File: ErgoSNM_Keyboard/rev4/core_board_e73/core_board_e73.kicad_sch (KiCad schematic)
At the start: 55 parts, among them J1 USB_C_Receptacle_USB2.0, J2 USB_C_Receptacle_USB2.0, J3 Conn_01x30, J4 Conn_Batt, J5 Debug, SW1 SW_DPDT_x2, U1 E73-2G4M08S1C, U2 SRV05-4, U3 TPS63020, U4 BQ24075RGT, U5 SRV05-4, Y1 32.768kHz

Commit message: feat: update USB ESD
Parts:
- removed R1, R2: 27R, Resistor_SMD:R_0402_1005Metric, symbol Device:R
- removed U2, U5: SRV05-4, Package_TO_SOT_SMD:SOT-23-6, symbol Power_Protection:SRV05-4
- added C1: 4.7nF, Capacitor_SMD:C_0805_2012Metric, symbol Device:C_Small
- added C4: 100nF, Capacitor_SMD:C_0402_1005Metric, symbol Device:C_Small
- added R1: 1M, Resistor_SMD:R_0603_1608Metric, symbol Device:R_Small
- added U2, U5: USBLC6-2SC6, Package_TO_SOT_SMD:SOT-23-6, symbol Power_Protection:USBLC6-2SC6
- R3, R4: value 5.1k -> 5.1k 1%
- renumbered C8 to C10, C9 to C11, C10 to C12, C11 to C13, C12 to C14, C13 to C15, C14 to C16, C15 to C17, C16 to C18, C17 to C19, C1 to C2, C2 to C3, C3 to C5, C4 to C6, C5 to C7, C6 to C8, C7 to C9, R14 to R2
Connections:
- net D+ is gone; now on net USB_D+: U1.31 (D+)
- net D- is gone; now on net USB_D-: U1.29 (D-)
- net GND: now also C1.2, C4.1, R1.2, U2.2 (GND), U5.2 (GND); no longer J1.S1 (SHIELD)
- net RX: now also U5.6 (I/O1); no longer J2.A7 (D-), J2.B7 (D-)
- net TX: now also U5.4 (I/O2); no longer J2.A6 (D+), J2.B6 (D+)
- net USB_D+: now also U2.4 (I/O2); no longer J1.A6 (D+), J1.B6 (D+)
- net USB_D-: now also U2.6 (I/O1); no longer J1.A7 (D-), J1.B7 (D-)
- net VBUS: now also C4.2, U2.5 (VBUS), U5.5 (VBUS)
- new net: J2.A6 (D+), J2.B6 (D+), U5.3 (I/O2)
- new net: J2.A7 (D-), J2.B7 (D-), U5.1 (I/O1)
- new net CONN_D+: J1.A6 (D+), J1.B6 (D+), U2.3 (I/O2)
- new net CONN_D-: J1.A7 (D-), J1.B7 (D-), U2.1 (I/O1)
- new net USB_SH: C1.1, J1.S1 (SHIELD), R1.1
- no-connect marks 28 -> 24
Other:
- note added: "Refer to Nordic nRF52833-DK 4.7nF 10V"

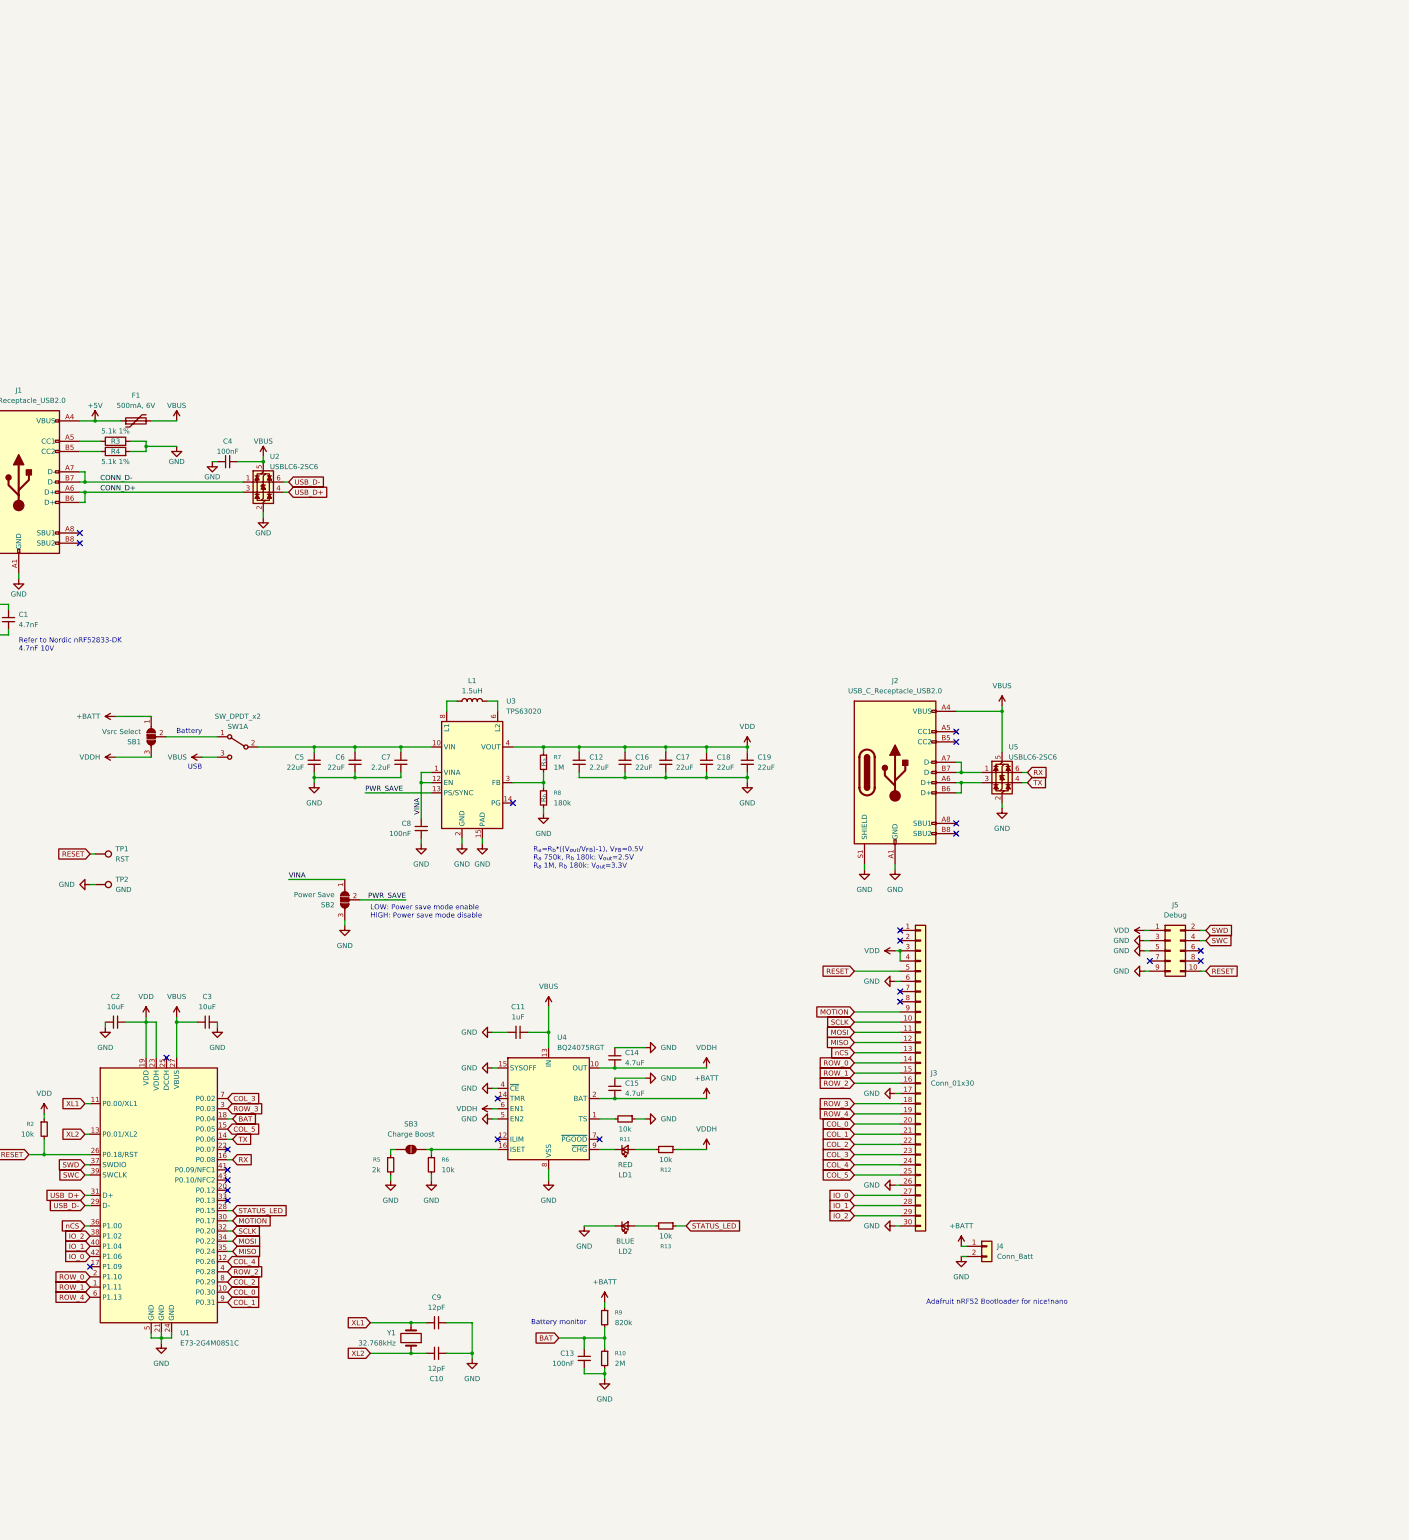
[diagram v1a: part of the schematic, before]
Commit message: feat: change Buck-Boost DC/DC IC from TPS63020 to TPS63900
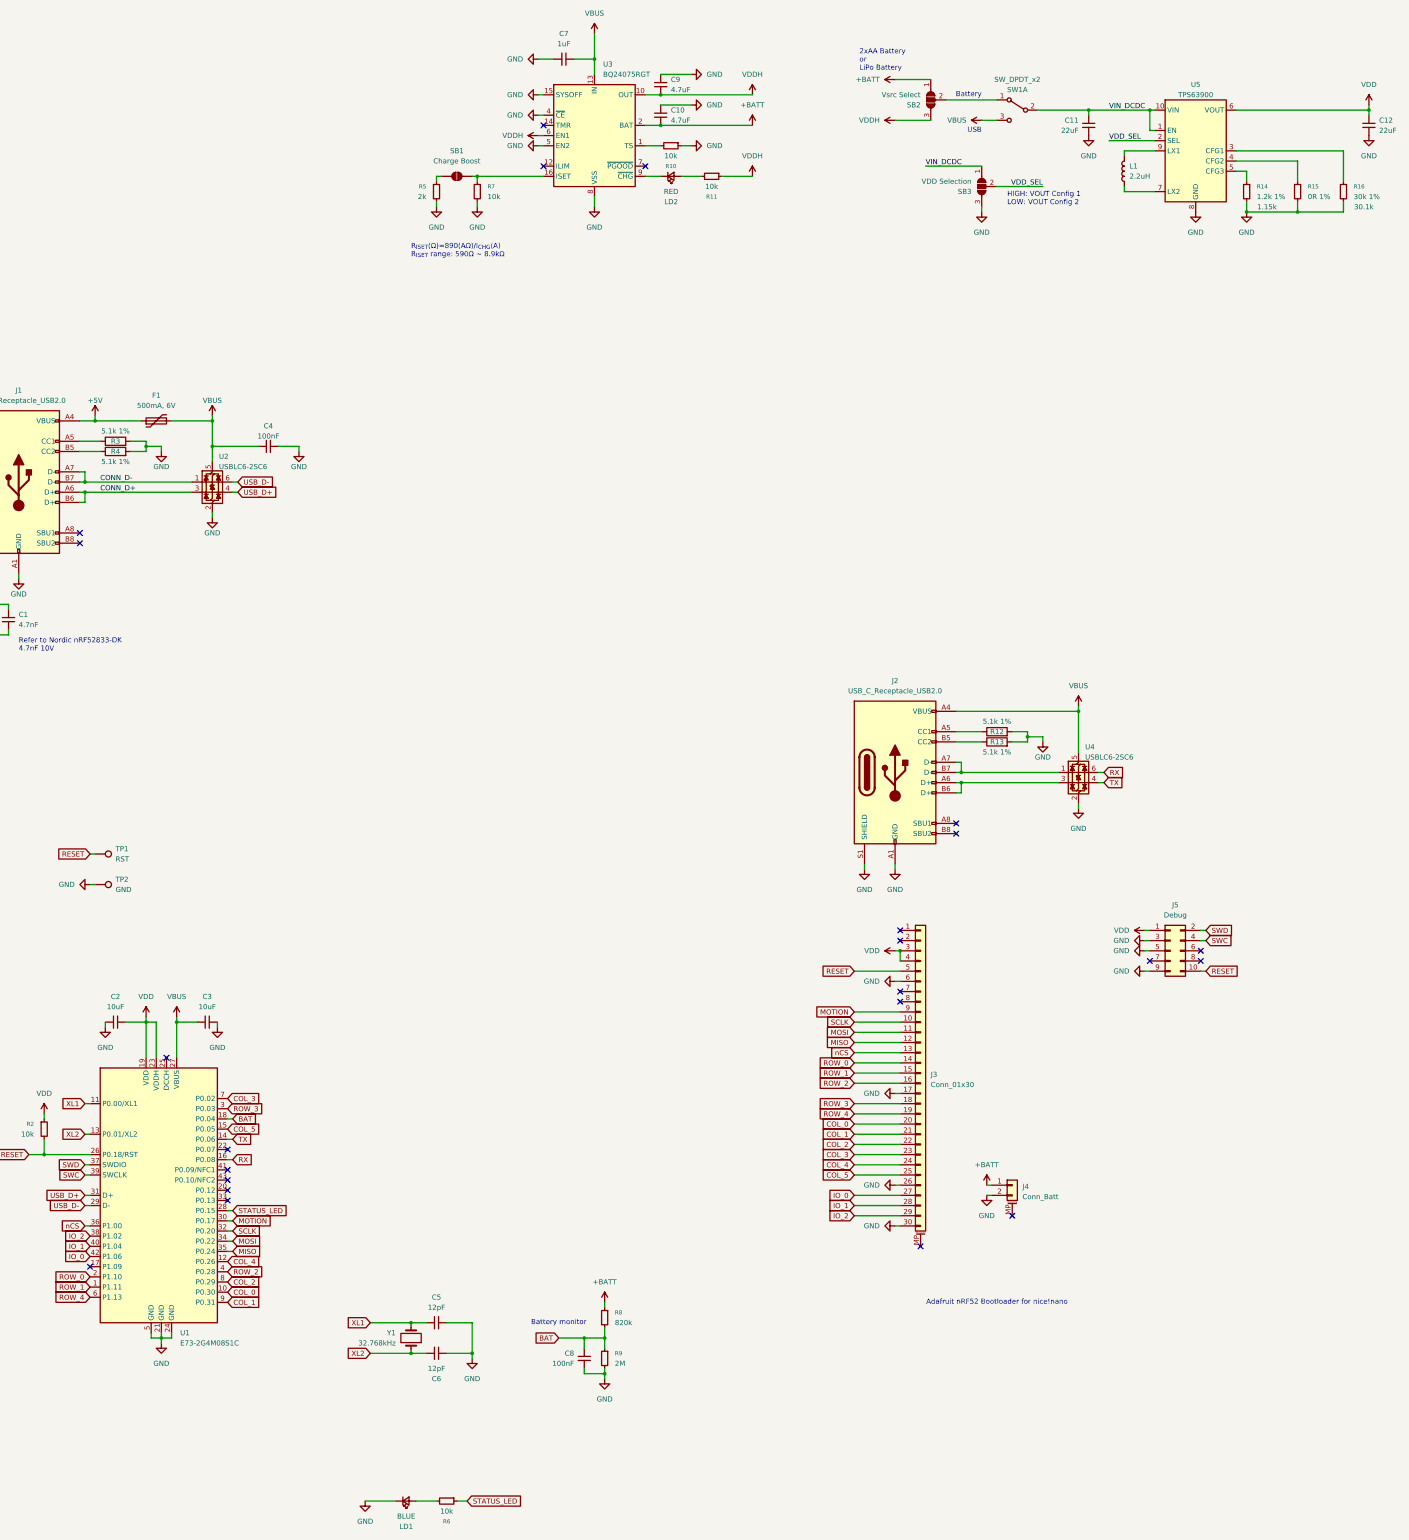
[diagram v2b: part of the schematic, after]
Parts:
- removed C16, C17, C18, C19, C5, C6: 22uF, Capacitor_SMD:C_0805_2012Metric, symbol Device:C_Small
- removed C7: 2.2uF, Capacitor_SMD:C_0603_1608Metric, symbol Device:C_Small
- removed C8: 100nF, Capacitor_SMD:C_0402_1005Metric, symbol Device:C_Small
- removed J4: Conn_Batt, Connector_JST:JST_PH_S2B-PH-SM4-TB_1x02-1MP_P2.00mm_Horizontal, symbol Connector_Generic:Conn_01x02
- removed R7: 1M, Resistor_SMD:R_0402_1005Metric, symbol Device:R_Small
- removed R8: 180k, Resistor_SMD:R_0402_1005Metric, symbol Device:R_Small
- removed U3: TPS63020, Package_SON:VSON-14-1EP_3x4.45mm_P0.65mm_EP1.6x4.2mm_ThermalVias, symbol ErgoSNM_Keyboard_Library:TPS63020
- added C11: 22uF, Capacitor_SMD:C_0805_2012Metric, symbol Device:C_Small
- added J4: Conn_Batt, Connector_JST:JST_PH_S2B-PH-SM4-TB_1x02-1MP_P2.00mm_Horizontal, symbol Connector_Generic_MountingPin:Conn_01x02_MountingPin
- added R12, R13: 5.1k 1%, Resistor_SMD:R_0402_1005Metric, symbol Device:R
- added R14: 1.2k 1%, Resistor_SMD:R_0603_1608Metric, symbol Device:R_Small
- added R15: 0R 1%, Resistor_SMD:R_0603_1608Metric, symbol Device:R_Small
- added R16: 30k 1%, Resistor_SMD:R_0603_1608Metric, symbol Device:R_Small
- added U5: TPS63900, Package_SON:WSON-10-1EP_2.5x2.5mm_P0.5mm_EP1.2x2mm, symbol Regulator_Switching:TPS63900
- C12: value 2.2uF -> 22uF; footprint Capacitor_SMD:C_0603_1608Metric -> Capacitor_SMD:C_0805_2012Metric; JLCPCB Part # C23630 -> C45783; MFR. Part # CL10A225KO8NNNC -> CL21A226MAQNNNE
- J3: symbol Connector_Generic:Conn_01x30 -> Connector_Generic_MountingPin:Conn_01x30_MountingPin
- L1: value 1.5uH -> 2.2uH; JLCPCB Part # C5832371 -> C5179446; MFR. Part # FTC252012S1R5MBCA -> FWP252012P-2R2ML
- SB3: renamed from SB2; value Power Save -> VDD Selection
- renumbered C15 to C10, C9 to C5, C10 to C6, C11 to C7, C13 to C8, C14 to C9, LD2 to LD1, LD1 to LD2, R11 to R10, R12 to R11, R13 to R6, R6 to R7, R9 to R8, R10 to R9, SB3 to SB1, SB1 to SB2, U4 to U3, U5 to U4
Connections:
- net VINA is gone; now on net VIN_DCDC: SB3.1 (A)
- net +BATT: now also J4.1 (Pin_1)
- net GND: now also C4.2, C11.2, J4.2 (Pin_2), R12.2, R13.2, R14.2, R15.2, R16.2, U5.11 (GND), U5.8 (GND); no longer C4.1
- net VBUS: now also C4.1; no longer C4.2
- net VDD: now also U5.6 (VOUT)
- net at L1.1: now also U5.7 (LX2)
- net at L1.2: now also U5.9 (LX1)
- net at J2.A5 (CC1): now also R12.1
- net at J2.B5 (CC2): now also R13.1
- net VIN_DCDC: now reaches SW1.2 (B)
- net VIN_DCDC: now also C11.1, U5.1 (EN), U5.10 (VIN)
- net PWR_SAVE renamed VDD_SEL
- net VDD_SEL: now also U5.2 (SEL)
- new net: R16.1, U5.3 (CFG1)
- new net: R15.1, U5.4 (CFG2)
- new net: R14.1, U5.5 (CFG3)
- no-connect marks 24 -> 23
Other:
- note added: "2xAA Battery or LiPo Battery"
- note added: "HIGH: VOUT Config 1 LOW: VOUT Config 2"
- note added: "R_{ISET}(Ω)=890(AΩ)/I_{CHG}(A) R_{ISET} range: 590Ω ~ 8.9kΩ"
- note removed: "LOW: Power save mode enable HIGH: Power save mode disable"
- note removed: "R_{a}=R_{b}*((V_{out}/V_{FB})-1), V_{FB}=0.5V R_{a} 750k, R_{b} 180k: V_{out}=2.5V R_{a} 1M, R_{b} 180k: V_{out}=3.3V"
- moved on the sheet: C10, C4, C7, C9, F1, LD1, LD2, R10, R11, R5, R6, R7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

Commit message: feat: change pin header position
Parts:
- removed J2: USB_C_Receptacle_USB2.0, Connector_USB:USB_C_Receptacle_HRO_TYPE-C-31-M-12, symbol Connector:USB_C_Receptacle_USB2.0
- removed J3: Conn_01x30, Connector_FFC-FPC:TE_3-1734839-0_1x30-1MP_P0.5mm_Horizontal, symbol Connector_Generic_MountingPin:Conn_01x30_MountingPin
- removed R12, R13: 5.1k 1%, Resistor_SMD:R_0402_1005Metric, symbol Device:R
- removed SW1: SW_DPDT_x2, ErgoSNM_Keyboard:MSKT-22D14-T, symbol Switch:SW_DPDT_x2
- removed U4: USBLC6-2SC6, Package_TO_SOT_SMD:SOT-23-6, symbol Power_Protection:USBLC6-2SC6
- added H23, H5, H6, H7: MountingHole, ErgoSNM_Keyboard:mouse_bit, symbol Mechanical:MountingHole
- added H4: MountingHole, MountingHole:MountingHole_2.7mm_M2.5_ISO7380, symbol Mechanical:MountingHole
- added J2, J3: Conn_02x10_Odd_Even, Connector_PinHeader_1.27mm:PinHeader_2x10_P1.27mm_Vertical_SMD, symbol Connector_Generic:Conn_02x10_Odd_Even
- added J4, J5: PJ-393_TRRS_8P, ErgoSNM_Keyboard:PJ-393 8P TRRS, symbol ErgoSNM_Keyboard_Library:PJ-393_TRRS_8P
- added J8, J9: Conn_02x05_Odd_Even, Connector_PinHeader_1.27mm:PinHeader_2x04_P1.27mm_Vertical, symbol Connector_Generic:Conn_02x04_Odd_Even
- added SB2: LiPo_CHG, Jumper:SolderJumper-2_P1.3mm_Open_TrianglePad1.0x1.5mm, symbol Jumper:SolderJumper_2_Open
- added SW1, SW2: SW_SPDT, ErgoSNM_Keyboard:9_3.5_3.5_switch, symbol Switch:SW_SPDT
- renumbered J4 to J6, J5 to J7, R14 to R12, R15 to R13, R16 to R14, SB2 to SB3, SB3 to SB4, U5 to U4
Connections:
- net +BATT: now also SB2.2 (B); no longer C10.2, U3.2 (BAT), U3.3 (BAT)
- net GND: now also SB4.1 (A), J3.2 (Pin_2), J3.20 (Pin_20), J4.T, J5.T; no longer SB4.3 (B)
- net RESET: now also J3.17 (Pin_17), J3.3 (Pin_3)
- net RX: now also J4.R2, J5.R1
- net TX: now also J4.R1, J5.R2
- net VBUS: now also J4.S, J5.S, SW1.3 (C), SW2.3 (C)
- net VDD: now also J3.1 (Pin_1), J3.19 (Pin_19)
- net VIN_DCDC: now also SB4.3 (B), SW1.2 (B), SW2.2 (B); no longer SB4.1 (A)
- net VBATT_SRC: now reaches SB3.2 (C)
- net VBATT_SRC: now also SW1.1 (A), SW2.1 (A)
- net COL_IO_4: now reaches U1.17 (P1.09)
- net COL_IO_4: now also J2.14 (Pin_14)
- net COL_IO_5: now reaches U1.22 (P0.07)
- net COL_IO_5: now also J2.16 (Pin_16)
- net COL_0 renamed COL_IO_2
- net COL_IO_2: now also J2.10 (Pin_10)
- net COL_1 renamed COL_IO_1
- net COL_IO_1: now also J2.8 (Pin_8)
- net COL_2 renamed COL_IO_0
- net COL_IO_0: now also J2.6 (Pin_6)
- net COL_3 renamed ROW_IO_5
- net ROW_IO_5: now also J2.15 (Pin_15)
- net COL_4 renamed HS_IO_0
- net HS_IO_0: now also J3.6 (Pin_6)
- net COL_5 renamed COL_IO_3
- net COL_IO_3: now also J2.12 (Pin_12)
- net IO_0: no longer names the net of U1.42 (P1.06)
- net IO_1: no longer names the net of U1.40 (P1.04)
- net IO_2: no longer names the net of U1.38 (P1.02)
- net MISO renamed HS_IO_1
- net HS_IO_1: now also J3.8 (Pin_8)
- net MOSI renamed HS_IO_2
- net HS_IO_2: now also J3.10 (Pin_10)
- net MOTION renamed HS_IO_4
- net HS_IO_4: now also J3.14 (Pin_14)
- net ROW_0 renamed ROW_IO_1
- net ROW_IO_1: now also J2.7 (Pin_7)
- net ROW_1 renamed ROW_IO_0
- net ROW_IO_0: now also J2.5 (Pin_5)
- net ROW_2 renamed ROW_IO_3
- net ROW_IO_3: now also J2.11 (Pin_11)
- net ROW_3 renamed ROW_IO_2
- net ROW_IO_2: now also J2.9 (Pin_9)
- net ROW_4 renamed ROW_IO_4
- net ROW_IO_4: now also J2.13 (Pin_13)
- net SCLK renamed HS_IO_3
- net HS_IO_3: now also J3.12 (Pin_12)
- net VDD_SEL renamed OUT_SEL
- net nCS renamed HS_IO_5
- net HS_IO_5: now also J3.16 (Pin_16)
- new net: C10.2, SB2.1 (A), U3.2 (BAT), U3.3 (BAT)
- no-connect marks 23 -> 38
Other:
- note removed: "Battery"

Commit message: feat: update the connectors of the main board and core board
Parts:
- removed LD1: BLUE, LED_SMD:LED_0603_1608Metric, symbol Device:LED_Small
- removed LD2: RED, LED_SMD:LED_0603_1608Metric, symbol Device:LED_Small
- C1: JLCPCB Part # C45783 -> C1744; MFR. Part # CL21A226MAQNNNE -> 0805B472K500NT
- C4: JLCPCB Part # (none) -> C1525; MFR. Part # (none) -> CL05B104KO5NNNC
- J2, J3, J7, J8, J9, TP1, TP2: now left out of the parts list
- J4, J5: JLCPCB Part # (none) -> C668609
- J6: JLCPCB Part # (none) -> C295747; MFR. Part # (none) -> S2B-PH-SM4-TB(LF)(SN)
- R1: JLCPCB Part # (none) -> C22935; MFR. Part # (none) -> 0603WAF1004T5E
- R10, R11, R2, R6, R7: JLCPCB Part # (none) -> C25744; MFR. Part # (none) -> 0402WGF1002TCE
- R13: JLCPCB Part # (none) -> C21189; MFR. Part # (none) -> 0603WAF0000T5E
- R14: JLCPCB Part # (none) -> C22984; MFR. Part # (none) -> 0603WAF3002T5E
- R3, R4: JLCPCB Part # (none) -> C25905; MFR. Part # (none) -> 0402WGF5101TCE
- R5: JLCPCB Part # (none) -> C4109; MFR. Part # (none) -> 0402WGF2001TCE
- R8: JLCPCB Part # (none) -> C2909386; MFR. Part # (none) -> FRC0402F8203TS
- R9: JLCPCB Part # (none) -> C11512; MFR. Part # (none) -> 0402WGF2004TCE
- U1: JLCPCB Part # (none) -> C356849; MFR. Part # (none) -> E73-2G4M08S1C
- U2: JLCPCB Part # (none) -> C2687116; MFR. Part # (none) -> USBLC6-2SC6
- U4: JLCPCB Part # (none) -> C1518762; MFR. Part # (none) -> TPS63900DSKR
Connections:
- net STATUS_LED: now also J2.2 (Pin_2), J2.20 (Pin_20); no longer U1.28 (P0.15)
- net VDDH: no longer R11.1
- net at U3.9 (~{CHG}): now also R11.2
- net CHG_LED: now reaches J2.18 (Pin_18)
- net CHG_LED: now also J2.4 (Pin_4), R11.1
- net at R6.2: now also U1.28 (P0.15)
- no-connect marks 38 -> 34
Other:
- moved on the sheet: R11, R6
